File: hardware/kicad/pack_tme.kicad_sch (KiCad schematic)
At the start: 129 parts, among them U1 MCP1640T-I/CHY

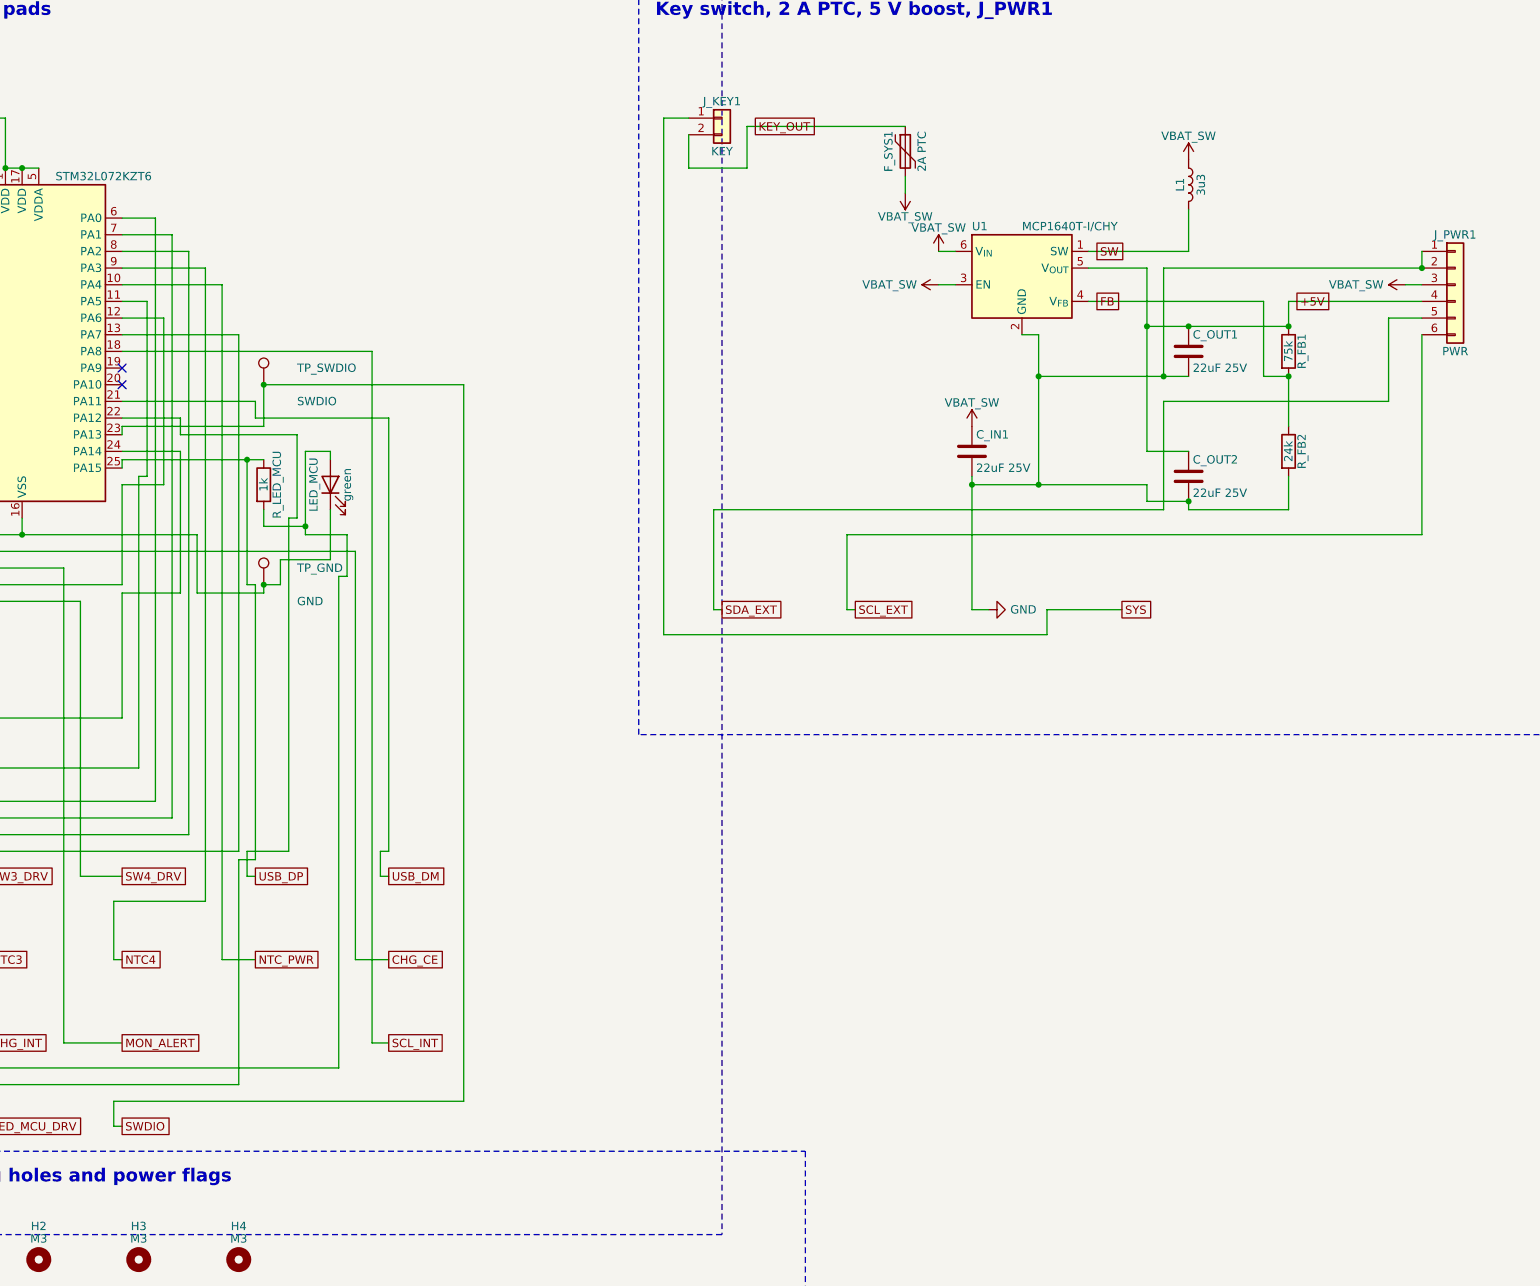
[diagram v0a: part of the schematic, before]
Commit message: hardware: UART debug header on all boards, I2C header and rail test pads on carrier, SDA/SCL pads on pack
Header is 1x3 2.54 mm (GND, MCU TX, MCU RX), hand-soldered, kept out of the BOM.
Carrier uses Heltec UART0 (GPIO43/44), STM32 boards USART1 (PA9/PA10).

Co-Authored-By: Claude Sonnet 5.5 <noreply@anthropic.com>
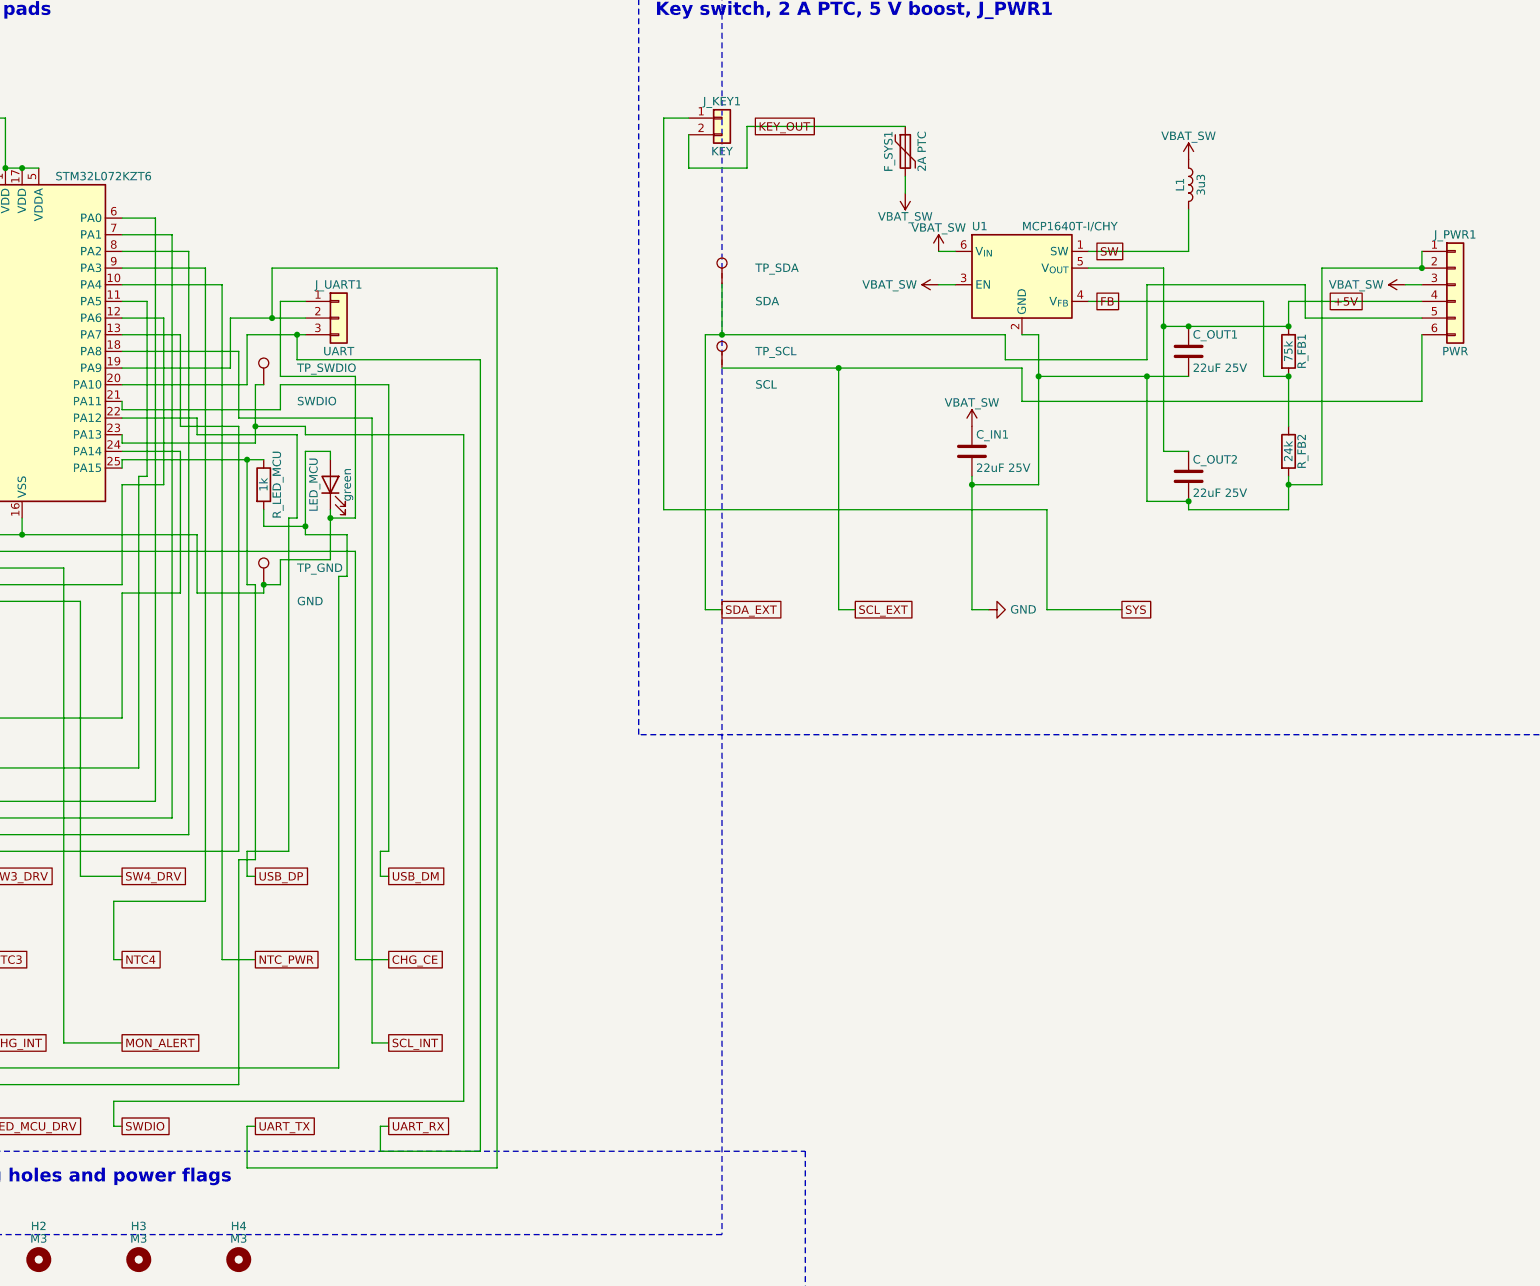
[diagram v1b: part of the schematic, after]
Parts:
- added J_UART1: UART, Connector_PinHeader_2.54mm:PinHeader_1x03_P2.54mm_Vertical, symbol Connector_Generic:Conn_01x03
- added TP_SCL: SCL, TestPoint:TestPoint_Pad_D1.5mm, symbol Connector:TestPoint
- added TP_SDA: SDA, TestPoint:TestPoint_Pad_D1.5mm, symbol Connector:TestPoint
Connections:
- net GND: now also J_UART1.1 (Pin_1)
- net SCL_EXT: now also TP_SCL.1
- net SDA_EXT: now also TP_SDA.1
- net UART_TX: now reaches U_MCU.19 (PA9)
- net UART_TX: now also J_UART1.2 (Pin_2)
- net UART_RX: now reaches U_MCU.20 (PA10)
- net UART_RX: now also J_UART1.3 (Pin_3)
- no-connect marks 8 -> 6

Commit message: hardware: KiCad 10 pipeline fixes, +5V reservoir caps, NS4168 1uF, pack UART header off the holders
KiCad 9 -> 10.0.7 broke the generators even on HEAD:
- gen_sch: libraries moved (hide yes) from effects to the property; read both,
  write it back into effects (KiCad 9 format), so hidden fields stop showing
  on every sheet and stop blocking the schematic router. Add the title block.
- gen_pcb: SetDoNotAllowCopperPour -> SetDoNotAllowZoneFills; copy the symbol's
  Datasheet/Description/Sim fields onto footprints (schematic parity now fails
  DRC); refuse THT pads under bottom-side parts (PTH_UNDER_OK allowlist).
- route.py: Power class routed at +40 um (Freerouting's octagons undercut 0.8 mm
  round ends, KiCad 10 exports no clearance margin), falling back to no margin
  if that leaves a connection unrouted; strip dangling stubs after SES import.
- pack: USB-C shield pin S1 -> SH; pack_tme: VSSOP-10 -> MSOP-10 footprint.

Design changes from the Konnect MCP review and datasheet check:
- carrier: C_5V1 10 uF + C_5V2 100 nF on +5V at J_PWR1 (no local cap before);
  C_AMP2 100 nF -> 1 uF per NS4168 datasheet (100 uF || 1 uF). carrier_tme
  places the new caps clear of its DAC.
- pack/pack_tme: J_UART1 sat under BT4 (bottom-side 18650 holder), caught by
  KiCad 10's pth_inside_courtyard; moved to the right strip, label in pin order.
  The NTC beads stay in the holder window (check ignored, gen_pcb enforces it).
- Docs: ORDERING counts, NS4168/TCA9534/BSS138/1N4148W datasheet check,
  TCA9534 P6/P7 firmware note.

All six boards: ERC 0, DRC 0 (0 unconnected, 0 parity), gerbers ok.

Co-Authored-By: Claude Opus 5.5 <noreply@anthropic.com>
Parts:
- U_MON1, U_MON2, U_MON3, U_MON4: footprint Package_SO:VSSOP-10_3x3mm_P0.5mm -> Package_SO:MSOP-10_3x3mm_P0.5mm
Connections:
- net GND: now also J_USB1.SH (SHIELD); no longer J_USB1.S1 (SHIELD)
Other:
- title: (none) -> AirsoftCounter v2 pack (hand-build)
- moved on the sheet: C_MCU3, C_VDDA
